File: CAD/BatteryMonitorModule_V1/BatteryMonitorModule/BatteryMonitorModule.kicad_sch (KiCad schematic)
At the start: 0 parts

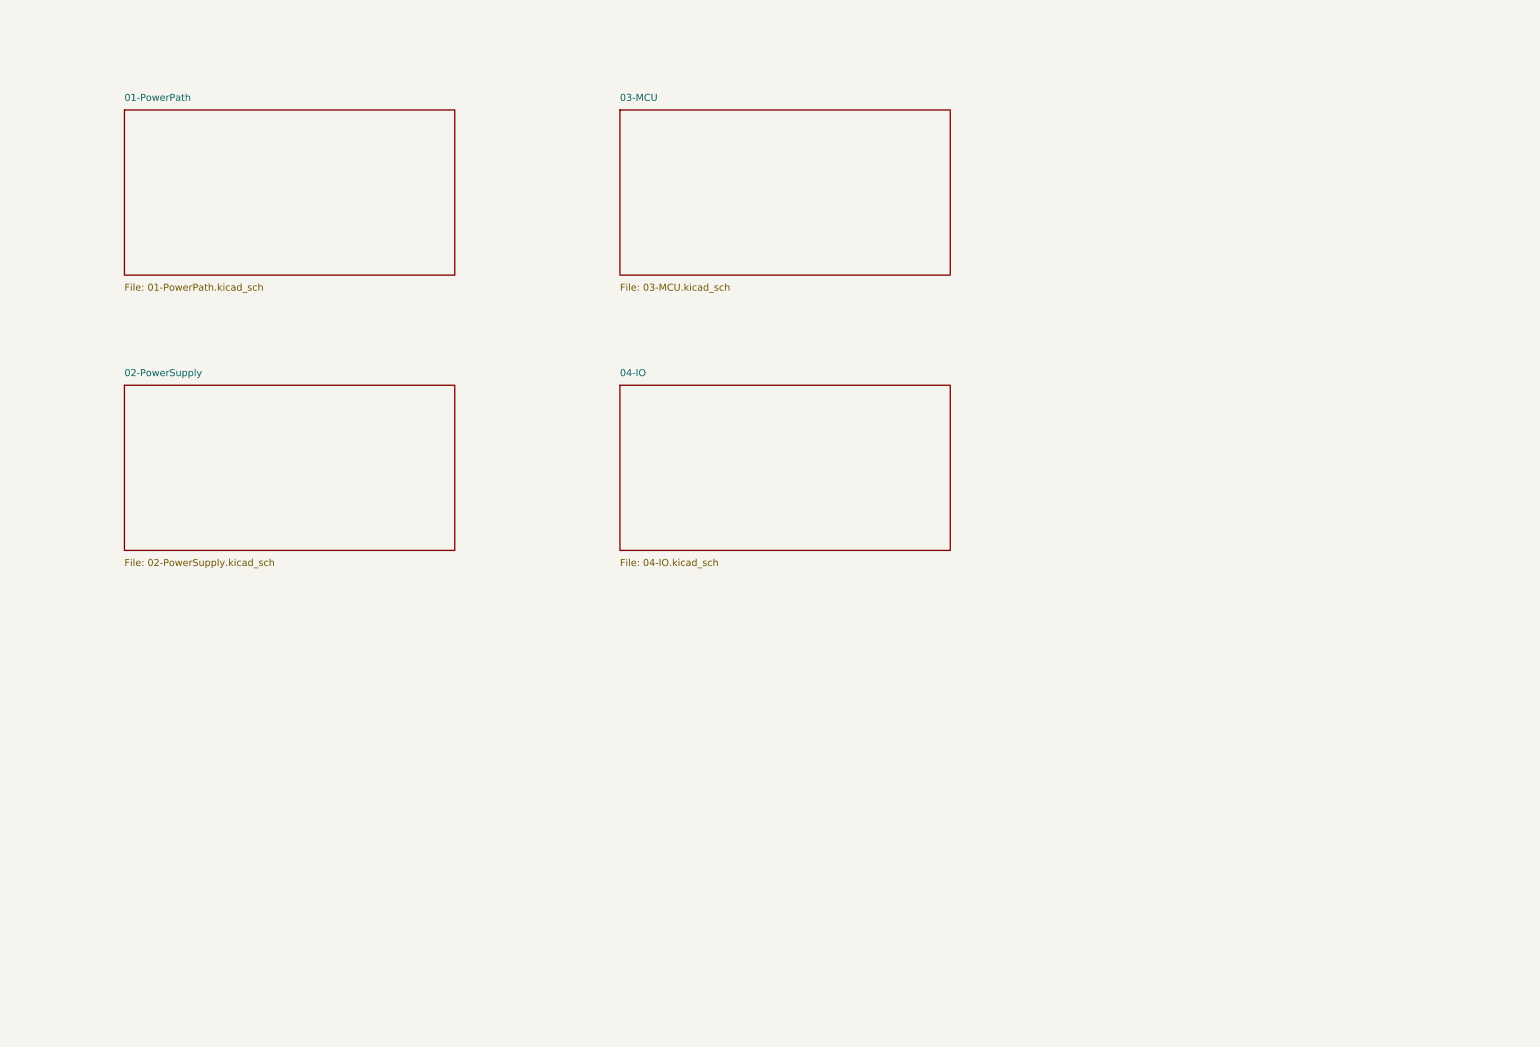
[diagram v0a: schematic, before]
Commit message: add QT06ADP83H0000G and UJ20-C USB-C connector symbols/footprints/3D models
Update V1 schematics (PowerPath, MCU, IO, top-level) to incorporate new parts.

Co-Authored-By: Claude Opus 4.7 (1M context) <noreply@anthropic.com>
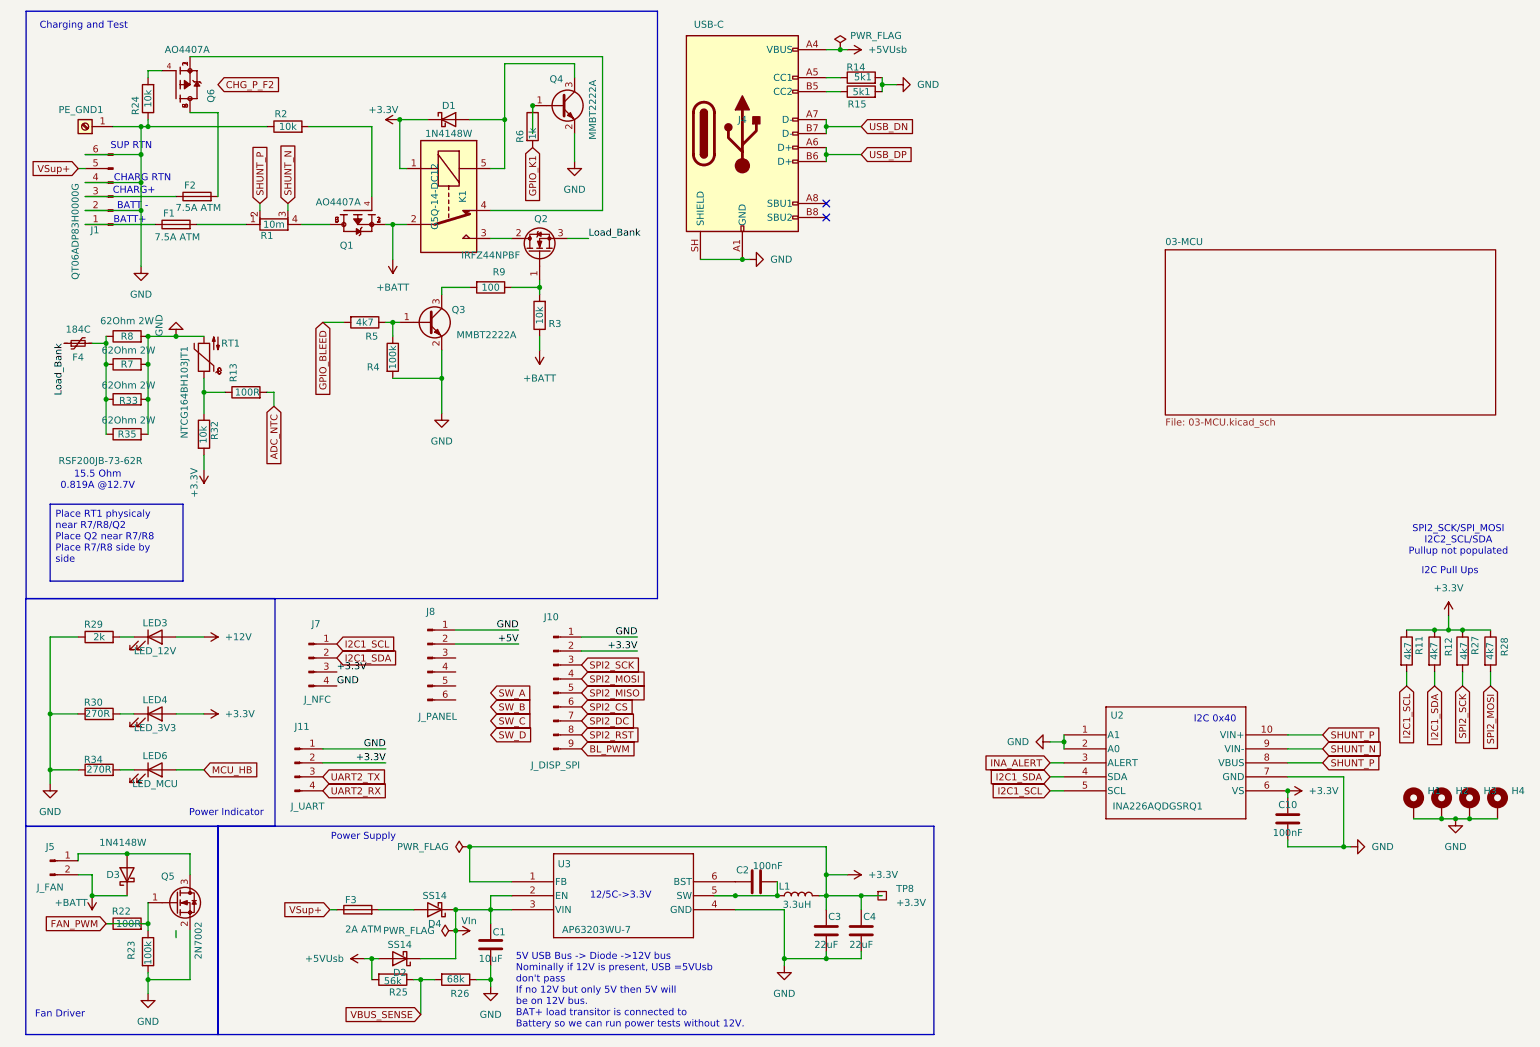
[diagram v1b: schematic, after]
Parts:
- added C1: 10uF, Capacitor_SMD:C_0805_2012Metric, symbol Device:C
- added C10, C2: 100nF, Capacitor_SMD:C_0603_1608Metric, symbol Device:C
- added C3, C4: 22uF, Capacitor_SMD:C_0805_2012Metric, symbol Device:C
- added D1, D3: 1N4148W, Diode_SMD:D_SOD-123, symbol Device:D_Schottky
- added D2, D4: SS14, Diode_SMD:D_SOD-123, symbol Device:D_Schottky
- added F1, F2: 7.5A ATM, BatteryMonitorModule_Custom:FUSE_BK-6013, symbol Device:Fuse
- added F3: 2A ATM, BatteryMonitorModule_Custom:FUSE_BK-6013, symbol Device:Fuse
- added F4: 184C, Resistor_THT:R_Axial_DIN0516_L15.5mm_D5.0mm_P20.32mm_Horizontal, symbol Device:Polyfuse_Small
- added H1, H2, H3, H4: MountingHole_Pad, symbol Mechanical:MountingHole_Pad
- added J1: QT06ADP83H0000G, BatteryMonitorModule_Custom:QT06ADP83H0000G, symbol Connector:Conn_01x06_Pin
- added J10: J_DISP_SPI, Connector_JST:JST_XH_B9B-XH-A_1x09_P2.50mm_Vertical, symbol Connector:Conn_01x09_Pin
- added J11: J_UART, Connector_PinHeader_2.54mm:PinHeader_1x04_P2.54mm_Vertical, symbol Connector:Conn_01x04_Pin
- added J4: USB-C, BatteryMonitorModule_Custom:SAMESKY_UJ20-C-H-G-SMT-1-P16-TR, symbol Connector:USB_C_Receptacle_USB2.0_16P
- added J5: J_FAN, Connector_PinHeader_2.54mm:PinHeader_1x02_P2.54mm_Vertical, symbol Connector:Conn_01x02_Pin
- added J7: J_NFC, Connector_JST:JST_XH_B4B-XH-A_1x04_P2.50mm_Vertical, symbol Connector:Conn_01x04_Pin
- added J8: J_PANEL, Connector_JST:JST_XH_B6B-XH-A_1x06_P2.50mm_Vertical, symbol Connector:Conn_01x06_Pin
- added K1: G5Q-14-DC12, Relay_THT:Relay_SPDT_Omron-G5Q-1, symbol Relay:G5Q-1
- added L1: 3.3uH, BatteryMonitorModule_Custom:IND_BOURNS_SRR4028, symbol Device:L
- added LED3: LED_12V, LED_SMD:LED_0603_1608Metric, symbol Device:LED
- added LED4: LED_3V3, LED_SMD:LED_0603_1608Metric, symbol Device:LED
- added LED6: LED_MCU, LED_SMD:LED_0603_1608Metric, symbol Device:LED
- added PE_GND1: Keystone 4966, BatteryMonitorModule_Custom:KEYSTONE_4966, symbol Connector:Screw_Terminal_01x01
- added Q1, Q6: AO4407A, AO4407A:SOIC127P600X175-8N, symbol AO4407A:AO4407A
- added Q2: IRFZ44NPBF, Package_TO_SOT_THT:TO-220-3_Vertical, symbol Transistor_FET:IRLZ44N
- added Q3, Q4: MMBT2222A, Package_TO_SOT_SMD:SOT-23, symbol Transistor_BJT:MMBT2222A
- added Q5: 2N7002, Package_TO_SOT_SMD:SOT-23, symbol Transistor_FET:BSS138
- added R1: 10m, Resistor_SMD:R_Shunt_Vishay_WSK2512_6332Metric_T2.21mm, symbol Device:R_Shunt
- added R11, R12, R27, R28, R5: 4k7, Resistor_SMD:R_0603_1608Metric, symbol Device:R
- added R13, R22: 100R, Resistor_SMD:R_0603_1608Metric, symbol Device:R
- added R14, R15: 5k1, Resistor_SMD:R_0603_1608Metric, symbol Device:R
- added R2, R24, R3, R32: 10k, Resistor_SMD:R_0603_1608Metric, symbol Device:R
- added R23, R4: 100k, Resistor_SMD:R_0603_1608Metric, symbol Device:R
- added R25: 56k, Resistor_SMD:R_0603_1608Metric, symbol Device:R
- added R26: 68k, Resistor_SMD:R_0603_1608Metric, symbol Device:R
- added R29: 2k, Resistor_SMD:R_0603_1608Metric, symbol Device:R
- added R30, R34: 270R, Resistor_SMD:R_0603_1608Metric, symbol Device:R
- added R33, R35, R7, R8: 62Ohm 2W, Resistor_THT:R_Axial_DIN0516_L15.5mm_D5.0mm_P5.08mm_Vertical, symbol Device:R
- added R6: 1k, Resistor_SMD:R_0603_1608Metric, symbol Device:R
- added R9: 100, Resistor_SMD:R_0603_1608Metric, symbol Device:R
- added RT1: NTCG164BH103JT1, Resistor_SMD:R_0603_1608Metric, symbol Device:Thermistor_NTC
- added TP8: +3.3V, TestPoint:TestPoint_Pad_2.0x2.0mm, symbol Connector:TestPoint_Square
- added U2: INA226AQDGSRQ1, Package_SO:MSOP-10_3x3mm_P0.5mm, symbol INA226AQDGSRQ1:INA226AQDGSRQ1
- added U3: AP63203WU-7, Package_TO_SOT_SMD:SOT-23-6_Handsoldering, symbol AP63205WU-7:AP63205WU-7
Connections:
- new net: F4.2, R33.1, R35.1, R7.1, R8.1
- new net: J4.A5 (CC1), R14.1
- new net: J4.B5 (CC2), R15.1
- new net: D4.2 (A), F3.2
- new net: Q3.1 (B), R4.1, R5.1
- new net: Q1.4, R2.2
- new net: Q1.5, Q1.6, Q1.7, Q1.8, R1.4
- new net: LED6.1 (K), R34.2
- new net: R13.1, R32.1, RT1.1
- new net: F1.1, J1.1 (Pin_1)
- new net: F2.1, J1.3 (Pin_3)
- new net: D1.2 (A), K1.5, Q4.3 (C)
- new net: F2.2, Q6.5, Q6.6, Q6.7, Q6.8
- new net: Q2.1 (G), R3.2, R9.1
- new net: Q3.3 (C), R9.2
- new net: K1.4, Q6.1, Q6.2, Q6.3
- new net: Q6.4, R24.2
- new net: Q4.1 (B), R6.1
- new net: D3.2 (A), J5.1 (Pin_1), Q5.3 (D)
- new net: C2.1, U3.6 (BST)
- new net: C2.2, L1.1, U3.5 (SW)
- new net: LED3.1 (K), R29.2
- new net: LED4.1 (K), R30.2
- new net: F1.2, R1.1
- new net: K1.3, Q2.2 (D)
- new net +12V: LED3.2 (A)
- new net +3.3V: C10.1, C3.1, C4.1, D1.1 (K), J10.2 (Pin_2), J11.2 (Pin_2), J7.3 (Pin_3), K1.1, L1.2, LED4.2 (A), R11.1, R12.1, R27.1, R28.1, R32.2, TP8.1, U2.6 (VS), U3.1 (FB)
- new net +5V: J8.2 (Pin_2)
- new net +5VUsb: D2.2 (A), J4.A4 (VBUS), J4.A9 (VBUS), J4.B4 (VBUS), J4.B9 (VBUS), R25.2
- new net +BATT: D3.1 (K), J5.2 (Pin_2), K1.2, Q1.1, Q1.2, Q1.3, R3.1
- new net ADC_NTC: R13.2
- new net BL_PWM: J10.9 (Pin_9)
- new net FAN_PWM: Q5.1 (G), R22.1, R22.2, R23.1
- new net GND: C1.2, C10.2, C3.2, C4.2, H1.1, H2.1, H3.1, H4.1, J1.2 (Pin_2), J1.4 (Pin_4), J1.6 (Pin_6), J10.1 (Pin_1), J11.1 (Pin_1), J4.A1 (GND), J4.A12 (GND), J4.B1 (GND), J4.B12 (GND), J4.SH (SHIELD), J7.4 (Pin_4), J8.1 (Pin_1), PE_GND1.1 (Pin_1), Q3.2 (E), Q4.2 (E), Q5.2 (S), R14.2, R15.2, R2.1, R23.2, R24.1, R26.1, R29.1, R30.1, R33.2, R34.1, R35.2, R4.2, R7.2, R8.2, RT1.2, U2.1 (A1), U2.2 (A0), U2.7 (GND), U3.4 (GND)
- new net GPIO_BLEED: R5.2
- new net GPIO_K1: R6.2
- new net I2C1_SCL: J7.1 (Pin_1), R11.2, U2.5 (SCL)
- new net I2C1_SDA: J7.2 (Pin_2), R12.2, U2.4 (SDA)
- new net INA_ALERT: U2.3 (ALERT)
- new net Load_Bank: F4.1, Q2.3 (S)
- new net MCU_HB: LED6.2 (A)
- new net SHUNT_N: R1.3, U2.9 (VIN-)
- new net SHUNT_P: R1.2, U2.10 (VIN+), U2.8 (VBUS)
- new net SPI2_CS: J10.6 (Pin_6)
- new net SPI2_DC: J10.7 (Pin_7)
- new net SPI2_MISO: J10.5 (Pin_5)
- new net SPI2_MOSI: J10.4 (Pin_4), R28.2
- new net SPI2_RST: J10.8 (Pin_8)
- new net SPI2_SCK: J10.3 (Pin_3), R27.2
- new net UART2_RX: J11.4 (Pin_4)
- new net UART2_TX: J11.3 (Pin_3)
- new net USB_DN: J4.A7 (D-), J4.B7 (D-)
- new net USB_DP: J4.A6 (D+), J4.B6 (D+)
- new net VBUS_SENSE: R25.1, R26.2
- new net VIn: C1.1, D2.1 (K), D4.1 (K), U3.2 (EN), U3.3 (VIN)
- new net VSup+: F3.1, J1.5 (Pin_5)
- no-connect marks 0 -> 2
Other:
- removed sheet 01-PowerPath
- removed sheet 02-PowerSupply
- removed sheet 04-IO
- note added: "12/5C->3.3V"
- note added: "15.5 Ohm 0.819A @12.7V"
- note added: "5V USB Bus -> Diode ->12V bus Nominally if 12V is present, USB =5VUsb don't pass If no 12V but only 5V then 5V will be on 12V bus. BAT+ load transitor is connected to Battery so we can run power tests without 12V."
- note added: "BATT -"
- note added: "BATT+"
- note added: "CHARG RTN"
- note added: "CHARG+"
- note added: "Charging and Test"
- note added: "Fan Driver"
- note added: "I2C 0x40"
- note added: "I2C Pull Ups"
- note added: "Power Indicator"
- note added: "Power Supply"
- note added: "SPI2_SCK/SPI_MOSI I2C2_SCL/SDA Pullup not populated"
- note added: "SUP RTN"

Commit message: add BatteryMonitorV2 STM32CubeMX project and V1 MCU schematic updates
Initial STM32CubeMX .ioc for BatteryMonitorV2. Update MCU schematic and
AP63205WU-7/INA226 custom symbols.

Co-Authored-By: Claude Opus 4.7 (1M context) <noreply@anthropic.com>
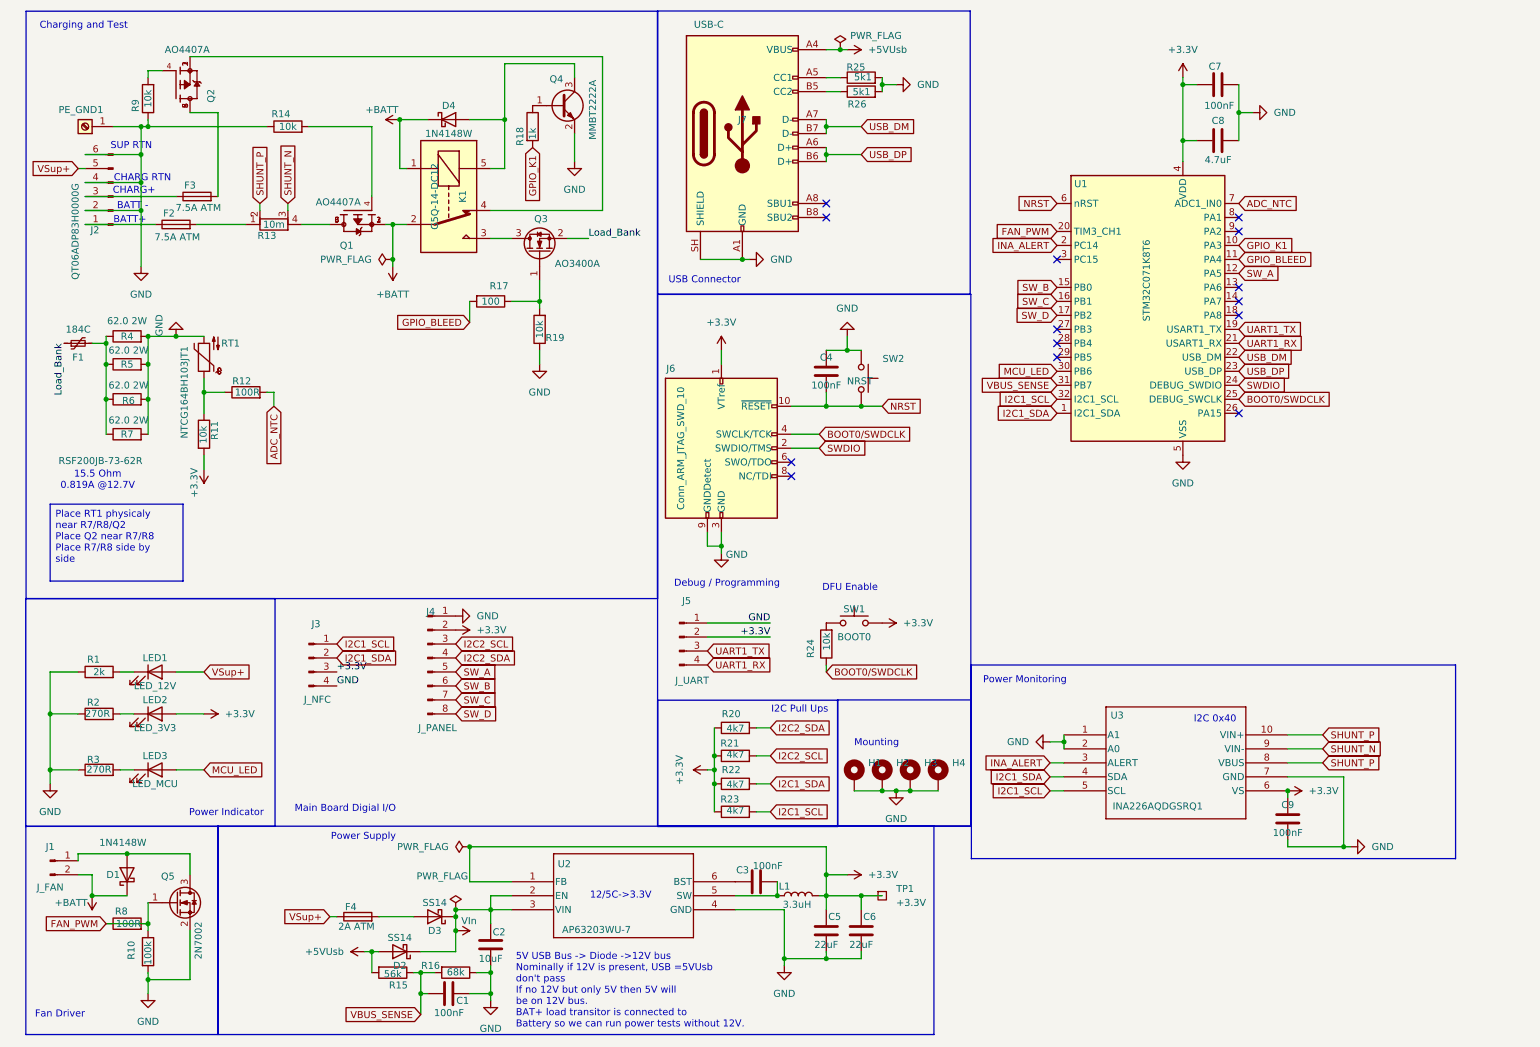
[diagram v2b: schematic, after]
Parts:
- removed J10: J_DISP_SPI, Connector_JST:JST_XH_B9B-XH-A_1x09_P2.50mm_Vertical, symbol Connector:Conn_01x09_Pin
- removed Q3: MMBT2222A, Package_TO_SOT_SMD:SOT-23, symbol Transistor_BJT:MMBT2222A
- removed R4: 100k, Resistor_SMD:R_0603_1608Metric, symbol Device:R
- removed R5: 4k7, Resistor_SMD:R_0603_1608Metric, symbol Device:R
- added C1: 100nF, Capacitor_SMD:C_0805_2012Metric, symbol Device:C
- added C4, C7: 100nF, Capacitor_SMD:C_0603_1608Metric, symbol Device:C
- added C8: 4.7uF, Capacitor_SMD:C_0805_2012Metric, symbol Device:C
- added J6: Conn_ARM_JTAG_SWD_10, Connector_PinHeader_2.00mm:PinHeader_2x03_P2.00mm_Vertical, symbol Connector:Conn_ARM_JTAG_SWD_10
- added R24: 10k, Resistor_SMD:R_0603_1608Metric, symbol Device:R
- added SW1: BOOT0, BatteryMonitorModule_Custom:SWITCH_FSMSM_TYC, symbol Switch:SW_Push
- added SW2: NRST, BatteryMonitorModule_Custom:SWITCH_FSMSM_TYC, symbol Switch:SW_Push
- added U1: STM32C071K8T6, Package_QFP:LQFP-32_7x7mm_P0.8mm, symbol MCU_ST_STM32C0:STM32C071K8Tx
- J4: renamed from J8; footprint Connector_JST:JST_XH_B6B-XH-A_1x06_P2.50mm_Vertical -> Connector_JST:JST_XH_B8B-XH-AM_1x08_P2.50mm_Vertical; symbol Connector:Conn_01x06_Pin -> Connector:Conn_01x08_Pin
- Q1: footprint AO4407A:SOIC127P600X175-8N -> Package_SO:SOIC-8_3.9x4.9mm_P1.27mm; KiLib_Generator package/gullwing -> (none)
- Q2: renamed from Q6; footprint AO4407A:SOIC127P600X175-8N -> Package_SO:SOIC-8_3.9x4.9mm_P1.27mm
- Q3: renamed from Q2; value IRFZ44NPBF -> AO3400A; footprint Package_TO_SOT_THT:TO-220-3_Vertical -> Package_TO_SOT_SMD:SOT-23; symbol Transistor_FET:IRLZ44N -> Transistor_FET:AO3400A
- R4: renamed from R8; value 62Ohm 2W -> 62.0 2W
- R5: renamed from R7; value 62Ohm 2W -> 62.0 2W
- R6: renamed from R33; value 62Ohm 2W -> 62.0 2W
- R7: renamed from R35; value 62Ohm 2W -> 62.0 2W
- renumbered C1 to C2, C2 to C3, C3 to C5, C4 to C6, C10 to C9, D3 to D1, D4 to D3, D1 to D4, F4 to F1, F1 to F2, F2 to F3, F3 to F4, J5 to J1, J1 to J2, J7 to J3, J11 to J5, J4 to J7, LED3 to LED1, LED4 to LED2, LED6 to LED3, R29 to R1, R23 to R10, R32 to R11, R13 to R12, R1 to R13, R2 to R14, R25 to R15, R26 to R16, R9 to R17, R6 to R18, R3 to R19, R30 to R2, R28 to R20, R27 to R21, R12 to R22, R11 to R23, R14 to R25, R15 to R26, R34 to R3, R22 to R8, R24 to R9, TP8 to TP1, U3 to U2, U2 to U3
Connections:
- net +12V is gone; now on net VSup+: LED1.2 (A)
- net +5V is gone; now on net +3.3V: J4.2 (Pin_2)
- net SPI2_MOSI is gone; now on net I2C2_SDA: R20.2
- net SPI2_SCK is gone; now on net I2C2_SCL: R21.2
- net +3.3V: now also C7.1, C8.1, J6.1 (VTref), SW1.2, U1.4 (VDD); no longer D4.1 (K), K1.1
- net +BATT: now also D4.1 (K), K1.1; no longer R19.1
- net ADC_NTC: now also U1.7 (PA0)
- net FAN_PWM: now also U1.20 (PC6)
- net GND: now also R19.1, C1.2, C4.1, C7.2, C8.2, J6.3 (GND), J6.5 (GND), J6.9 (GNDDetect), SW2.1, U1.5 (VSS)
- net GPIO_BLEED: now also R17.2, U1.11 (PA4)
- net GPIO_K1: now also U1.10 (PA3)
- net I2C1_SCL: now also U1.32 (PB8)
- net I2C1_SDA: now also U1.1 (PB9)
- net INA_ALERT: now also U1.2 (PC14)
- net Load_Bank: now also Q3.2 (S); no longer Q3.3 (S)
- net SW_A: now also J4.5 (Pin_5), U1.12 (PA5)
- net SW_B: now also J4.6 (Pin_6), U1.15 (PB0)
- net SW_C: now also J4.7 (Pin_7), U1.16 (PB1)
- net SW_D: now also J4.8 (Pin_8), U1.17 (PB2)
- net USB_DP: now also U1.23 (PA12)
- net VBUS_SENSE: now also C1.1, U1.31 (PB7)
- net I2C2_SCL: now reaches J4.3 (Pin_3)
- net I2C2_SDA: now reaches J4.4 (Pin_4)
- net at K1.3: now also Q3.3 (D); no longer Q3.2 (D)
- net MCU_HB renamed MCU_LED
- net MCU_LED: now also U1.30 (PB6)
- net UART2_RX renamed UART1_RX
- net UART1_RX: now also U1.21 (PA10)
- net UART2_TX renamed UART1_TX
- net UART1_TX: now also U1.19 (PA9)
- net USB_DN renamed USB_DM
- net USB_DM: now also U1.22 (PA11)
- new net: R24.2, SW1.1
- new net BOOT0/SWDCLK: J6.4 (SWCLK/TCK), R24.1, U1.25 (PA14)
- new net NRST: C4.2, J6.10 (~{RESET}), SW2.2, U1.6 (PF2)
- new net SWDIO: J6.2 (SWDIO/TMS), U1.24 (PA13)
- no-connect marks 2 -> 14
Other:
- removed sheet 03-MCU
- note added: "DFU Enable"
- note added: "Debug / Programming"
- note added: "Main Board Digial I/O"
- note added: "Mounting"
- note added: "Power Monitoring"
- note added: "USB Connector"
- note removed: "SPI2_SCK/SPI_MOSI I2C2_SCL/SDA Pullup not populated"
- moved on the sheet: D2, D3, F4, H1, H2, H3, H4, J5, LED1, R1, R15, R16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

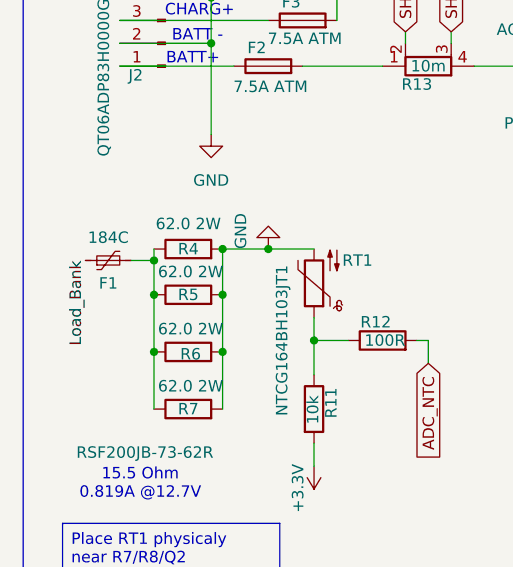
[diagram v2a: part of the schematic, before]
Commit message: assign M3 mounting hole footprints and rename F1 to TF1
Co-Authored-By: Claude Opus 4.7 (1M context) <noreply@anthropic.com>
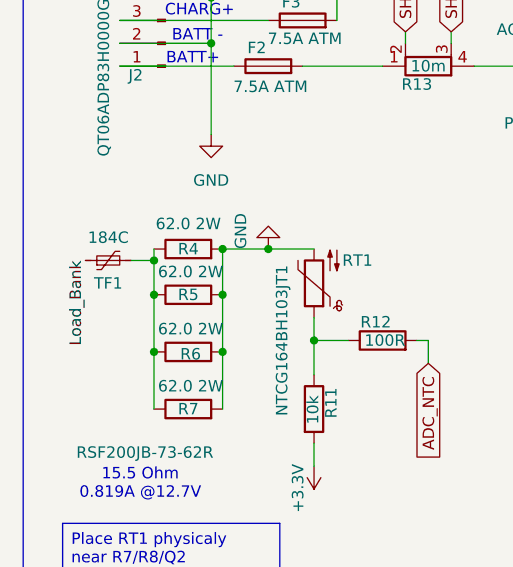
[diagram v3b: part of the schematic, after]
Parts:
- H1, H2, H3, H4: footprint (none) -> MountingHole:MountingHole_3.2mm_M3_DIN965_Pad
- renumbered F1 to TF1
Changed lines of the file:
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@@
 			)
 		)
-		(property "Footprint" ""
+		(property "Footprint" "MountingHole:MountingHole_3.2mm_M3_DIN965_Pad"
 			(at 167.64 151.13 0)
 			(hide yes)
@@
 			)
 		)
-		(property "Footprint" ""
+		(property "Footprint" "MountingHole:MountingHole_3.2mm_M3_DIN965_Pad"
 			(at 172.72 151.13 0)
 			(hide yes)
@@
 			)
 		)
-		(property "Footprint" ""
+		(property "Footprint" "MountingHole:MountingHole_3.2mm_M3_DIN965_Pad"
 			(at 162.56 151.13 0)
 			(hide yes)
@@
 		(in_pos_files yes)
 		(dnp no)
-		(property "Reference" "F1"
+		(property "Reference" "TF1"
 			(at 21.59 74.93 90)
 			(show_name no)
@@
 			(project "BatteryMonitorModule"
 				(path "/03269402-9c05-492f-98b8-b4c760268d66"
-					(reference "F1")
+					(reference "TF1")
 					(unit 1)
 				)
@@
 			)
 		)
-		(property "Footprint" ""
+		(property "Footprint" "MountingHole:MountingHole_3.2mm_M3_DIN965_Pad"
 			(at 177.8 151.13 0)
 			(hide yes)
